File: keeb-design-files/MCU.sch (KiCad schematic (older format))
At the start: 36 parts, among them J1 Conn_ARM_JTAG_SWD_10, J2 SMA, J6 Conn_01x04, SW1 RESET, SW70 BOOT0, U1 STM32L452CEUx, U2 nRF24L01P, Y2 Crystal_GND24

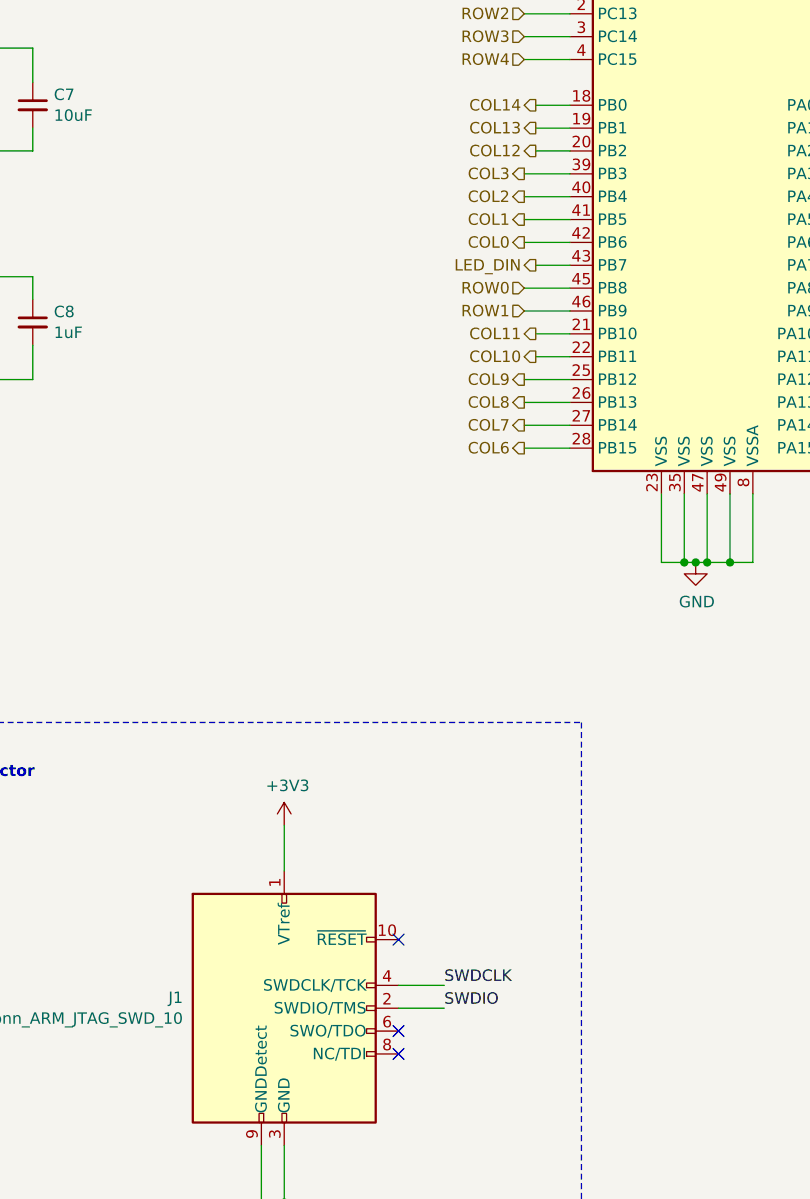
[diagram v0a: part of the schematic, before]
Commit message: More routing added planes and re-wired MCU a bit
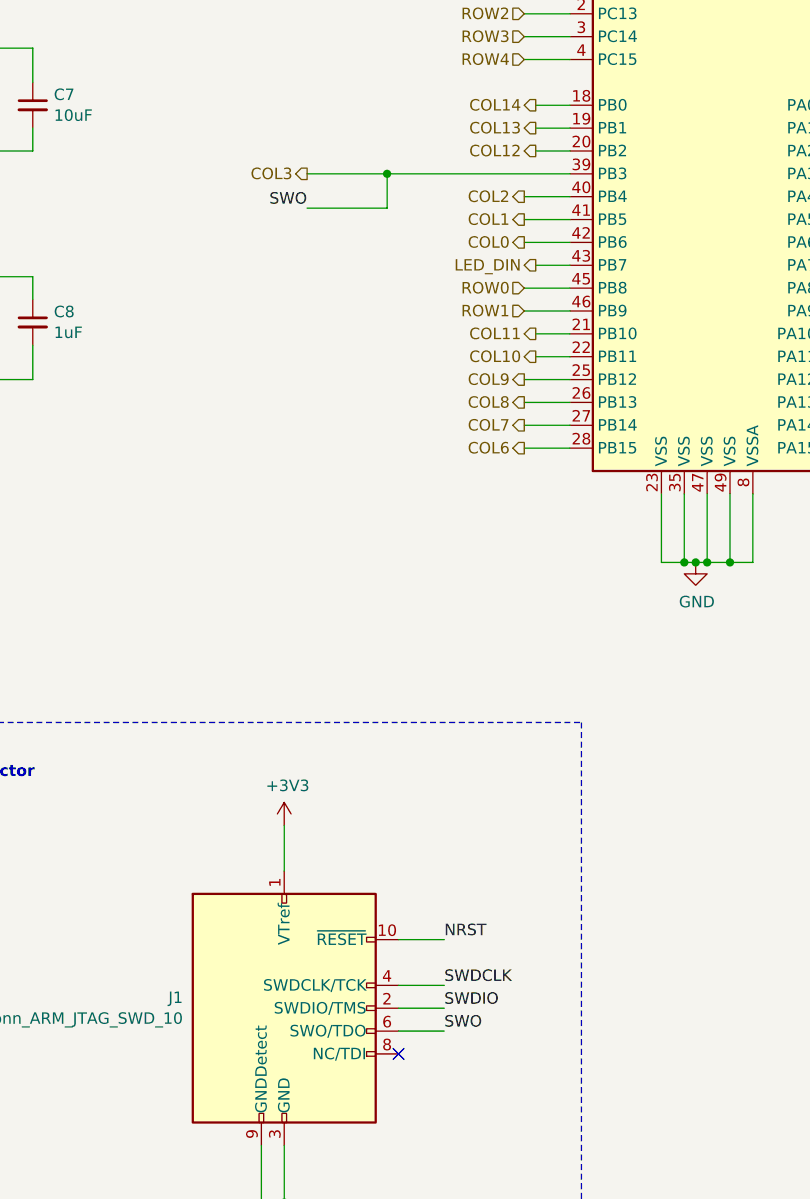
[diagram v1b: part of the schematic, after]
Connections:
- net COL3: now also J1.6 (SWO/TDO)
- net NRST: now also J1.10 (~RESET~)
- no-connect marks 5 -> 3
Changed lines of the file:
@@
 Text HLabel 3650 3050 0    50   Output ~ 0
 COL2
-Text HLabel 3650 2950 0    50   Output ~ 0
+Text HLabel 2700 2950 0    50   Output ~ 0
 COL3
 Text HLabel 5350 4150 2    50   Output ~ 0
@@
 	3850 2850 3700 2850
 Wire Wire Line
-	3850 2950 3650 2950
+	3850 2950 3050 2950
 Wire Wire Line
 	3850 3050 3650 3050
@@
 Text Label 5250 3250 0    50   ~ 0
 SPI_MISO
-NoConn ~ 3100 6300
-NoConn ~ 3100 6700
 NoConn ~ 3100 6800
 Text Label 3450 2050 0    50   ~ 0
@@
 	3650 3950 3850 3950
 NoConn ~ 5050 2850
+Text Label 3300 6700 0    50   ~ 0
+SWO
+Wire Wire Line
+	3300 6700 3100 6700
+Text Label 2700 3100 2    50   ~ 0
+SWO
+Wire Wire Line
+	2700 3100 3050 3100
+Wire Wire Line
+	3050 3100 3050 2950
+Connection ~ 3050 2950
+Wire Wire Line
+	3050 2950 2700 2950
+Text Label 3300 6300 0    50   ~ 0
+NRST
+Wire Wire Line
+	3300 6300 3100 6300
 $EndSCHEMATC

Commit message: Create gerbers picknplace and bom
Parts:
- C14, C15: LCSC Part Number C70464 -> C1555
- C19: LCSC Part Number C318581 -> C1550
- L2: LCSC Part Number C77121 -> C27123
- L3: LCSC Part Number C77123 -> C13818
- U1: LCSC Part Number (none) -> C222355
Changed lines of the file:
@@
 F 2 "Inductor_SMD:L_0402_1005Metric" H 9500 1650 50  0001 C CNN
 F 3 "~" H 9500 1650 50  0001 C CNN
-F 4 "C77121" H 9500 1650 50  0001 C CNN "LCSC Part Number"
+F 4 "C27123" H 9500 1650 50  0001 C CNN "LCSC Part Number"
 	1    9500 1650
 	0    -1   -1   0
@@
 F 2 "Inductor_SMD:L_0402_1005Metric" H 9500 2200 50  0001 C CNN
 F 3 "~" H 9500 2200 50  0001 C CNN
-F 4 "C77123" H 9500 2200 50  0001 C CNN "LCSC Part Number"
+F 4 "C13818" H 9500 2200 50  0001 C CNN "LCSC Part Number"
 	1    9500 2200
 	0    -1   -1   0
@@
 F 2 "Capacitor_SMD:C_0402_1005Metric" H 10250 2400 50  0001 C CNN
 F 3 "~" H 10250 2400 50  0001 C CNN
-F 4 "C318581" H 10250 2400 50  0001 C CNN "LCSC Part Number"
+F 4 "C1550" H 10250 2400 50  0001 C CNN "LCSC Part Number"
 	1    10250 2400
 	1    0    0    -1
@@
 F 2 "Capacitor_SMD:C_0402_1005Metric" H 9300 3450 50  0001 C CNN
 F 3 "~" H 9300 3450 50  0001 C CNN
-F 4 "C70464" H 9300 3450 50  0001 C CNN "LCSC Part Number"
+F 4 "C1555" H 9300 3450 50  0001 C CNN "LCSC Part Number"
 	1    9300 3450
 	1    0    0    -1
@@
 F 2 "Capacitor_SMD:C_0402_1005Metric" H 9000 3450 50  0001 C CNN
 F 3 "~" H 9000 3450 50  0001 C CNN
-F 4 "C70464" H 9000 3450 50  0001 C CNN "LCSC Part Number"
+F 4 "C1555" H 9000 3450 50  0001 C CNN "LCSC Part Number"
 	1    9000 3450
 	1    0    0    -1
@@
 F 2 "Package_DFN_QFN:QFN-48-1EP_7x7mm_P0.5mm_EP5.6x5.6mm" H 3950 1450 50  0001 R CNN
 F 3 "http://www.st.com/st-web-ui/static/active/en/resource/technical/document/datasheet/DM00340549.pdf" H 4450 2850 50  0001 C CNN
+F 4 "C222355" H 4450 2850 50  0001 C CNN "LCSC Part Number"
 	1    4450 2850
 	1    0    0    -1
